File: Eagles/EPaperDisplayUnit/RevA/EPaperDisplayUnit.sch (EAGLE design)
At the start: 93 parts, among them IC1 AT25, IC2 LT1763CS8-3.3, Q1 SI3481DV, Q2 SI3481DV, U1 2N7002BK, U2 LPC824M201JHI33, X2 FH12-50S-0.5SH

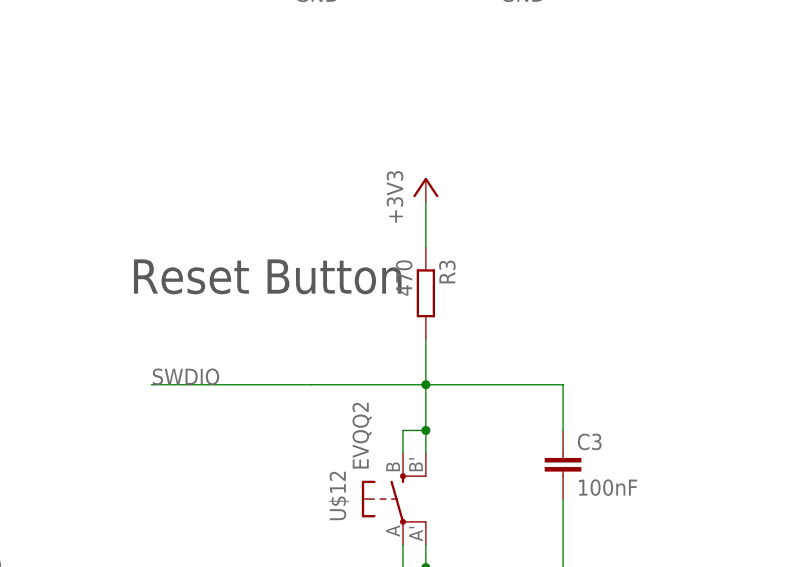
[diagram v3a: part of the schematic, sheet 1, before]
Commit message: [Draw schematic for the display unit #8]
fix a full up res value
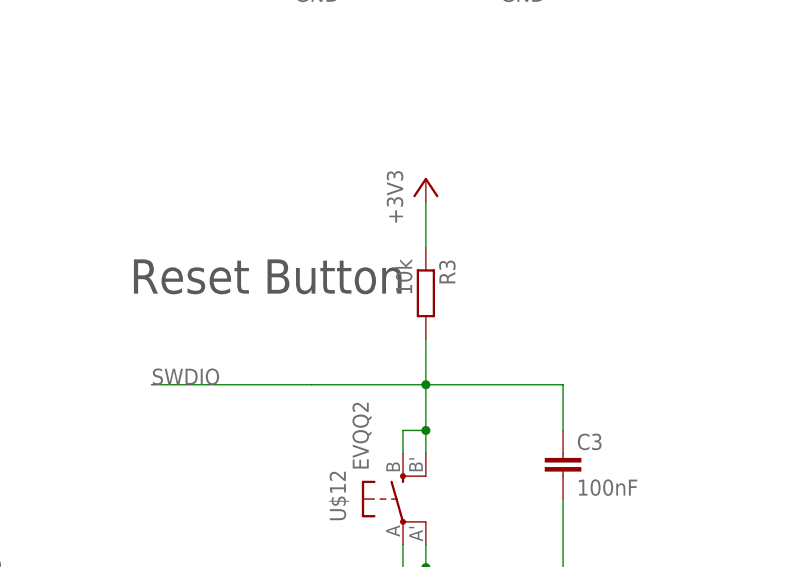
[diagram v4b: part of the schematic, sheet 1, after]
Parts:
- R3: value 470 -> 10k
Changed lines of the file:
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@@
 <part name="U$12" library="adafruit" deviceset="EVQQ2" device=""/>
 <part name="C3" library="rcl" deviceset="C-EU" device="C0603" value="100nF"/>
-<part name="R3" library="resistor" deviceset="R-EU_" device="R0402" value="470"/>
+<part name="R3" library="resistor" deviceset="R-EU_" device="R0402" value="10k"/>
 <part name="VSYS2" library="supply1" deviceset="+3V3" device=""/>
 <part name="VSYS3" library="supply1" deviceset="+3V3" device=""/>

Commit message: [Draw schematic for the display unit #8]
change resistors and caps to 0402 package to save space on the upcoming PCB
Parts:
- removed C27, C29: 10n, rcl:C-EUC0603
- removed C28, C30: 1u, rcl:C-EUC0603
- removed R11: 100K, resistor:R-EU_R0603
- removed R12: 47K, rcl:R-EU_R0603
- added C38, C40, C41: 2u2, rcl:C-EUC0402
- added C39: 10uF, rcl:C-EUC0402
- added R16: 22k, resistor:R-EU_R0402
- added R17: 47k, resistor:R-EU_R0402
- C1, C2: value (none) -> 16pF; device adafruit:C-USC0603 -> rcl:C-EUC0402
- C10, C11, C12, C13, C14, C15, C16, C17, C20, C21: device rcl:C-EUC1608 -> rcl:C-EUC0402
- C18: value 2u2 -> 10uF; device rcl:C-EUC1608 -> rcl:C-EUC0402
- C19: value 10u -> 10uF; device rcl:C-EUC1608 -> rcl:C-EUC0402
- C22, C31: value 2u2 -> 10nF; device rcl:C-EUC1608 -> rcl:C-EUC0402
- C23: value 2u2 -> 1uF; device rcl:C-EUC1608 -> rcl:C-EUC0402
- C24: value 10n -> 1uF; device resistor:C-EUC0603 -> eagle-ltspice:CC0402
- C25: value 10n -> 10nF; device rcl:C-EUC0603 -> rcl:C-EUC0402
- C26: value 100n -> 10nF; device rcl:C-EUC0603 -> eagle-ltspice:CC0402
- C32: value 2u2 -> 100nF; device rcl:C-EUC1608 -> rcl:C-EUC0402
- C33, C34: value 10u -> 2u2; device rcl:C-EUC1608 -> rcl:C-EUC0402
- C35: value 100nF -> 10nF; device rcl:C-EUC0603 -> rcl:C-EUC0402
- C36: value 10nF -> 1uF; device rcl:C-EUC0603 -> rcl:C-EUC0402
- C5: device rcl:C-EUC0603 -> rcl:C-EUC0402
- C7: value 100uF -> 100nF; device rcl:C-EUC0603 -> rcl:C-EUC0402
- C8: value 2.2 -> 2u2; device rcl:C-EUC0603 -> rcl:C-EUC0402
- C9: value 1uF -> 100uF; device rcl:C-EUC0603 -> rcl:C-EUC0402
- IC1: value AT25 -> AT25P; device atmel:AT25 -> atmel:AT25P
- R10: device rcl:R-EU_R0603 -> resistor:R-EU_R0402
- R13: value 47k -> 100k; device resistor:R-EU_R0603 -> resistor:R-EU_R0402
- R14: value 22k -> 47k; device resistor:R-EU_R0603 -> resistor:R-EU_R0402
- R15: value 2k2 -> 22k; device rcl:R-EU_R0603 -> resistor:R-EU_R0402
- R6: value 22k -> 100k; device resistor:R-EU_R0603 -> resistor:R-EU_R0402
- R7: value (none) -> 10k; device rcl:R-EU_R0603 -> resistor:R-EU_R0402
- R8: value 100k -> 2.2; device rcl:R-EU_R0603 -> resistor:R-EU_R0402
- R9: value 10k -> 2k2; device rcl:R-EU_R0603 -> resistor:R-EU_R0402
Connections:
- net !TCM_BUSY: now also R14.1; no longer R12.1
- net !TCM_EN: now also R16.2; no longer R6.1
- net +3V3: now also C7.2, C9.2, R16.1; no longer C35.1, C7.1, R6.2
- net ADC_TEMP: now also C25.1, R15.2, R17.1; no longer C24.2, R13.1, R14.2
- net DC_PWR_EN: now also R7.2; no longer R9.2
- net DISCHARGE_VCC: now also R9.1; no longer R15.1
- net GND: now also C1.1, C18.1, C2.1, C20.1, C21.1, C22.1, C23.1, C24.2, C36.2, C39.1, C40.1, C41.1, C5.1, C7.1, C8.1, C9.1, R15.1, R7.1; no longer C20.2, C21.2, C22.2, C23.2, C24.1, C27.2, C28.2, C29.2, C30.2, C5.2, C7.2, C8.2, R14.1, R9.1
- net N$11: now also R6.2; no longer R8.2
- net N$12: now also R6.1, R8.2; no longer R7.2, R8.1
- net N$19: now also C2.2
- net N$20: now also C1.2
- net N$31: now also C38.1; no longer C18.1
- net N$32: now also C38.2; no longer C18.2
- net N$36: now also C18.2, R10.2; no longer C19.2, R10.1
- net N$37: now also R10.1; no longer R10.2
- net N$6: now also C22.2
- net N$9: now also C20.2; no longer C8.1
- net TC_BOOT/DISCHARGE_VDL: now also R13.1; no longer R11.1
- net VBATT: now also C23.2
- net VCC: now also C19.2, C39.2, C5.2, R9.2; no longer C33.2, C34.2, C5.1, R15.2
- net VDD: now also C24.1, C31.1, C32.1, C35.1, C36.1, R14.2, R17.2, R8.1; no longer C25.1, C27.1, C28.1, C29.1, C30.1, R11.2, R12.2, R7.1
- net VDH: now also C33.2; no longer C20.1
- net VDL: now also C34.2; no longer C21.1
- net VGH: now also C21.2, C40.2; no longer C22.1, C31.1
- net VGL: now also C41.2, C8.2; no longer C23.1, C32.1
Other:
- moved on the sheet: C1, C18, C19, C2, C20, C21, C22, C23, C24, C25, C26, C33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

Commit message: Board design committing
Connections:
- removed net N$2: U$23.1
- removed net N$41: IC2.SENSE
- removed net N$48: C3.1, R3.2, U$12.S, U$12.S1
- net +3V3: now also D4.C
- net N$19: now also U$3.2
- net N$20: now also U$3.1
- net N$5: now also U$23.1
- net N$6: now also IC2.SENSE
- net SWDIO: now also C3.1, R3.2, U$12.S, U$12.S1
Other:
- moved on the sheet: TP10, U$6
